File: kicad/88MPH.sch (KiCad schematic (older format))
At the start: 22 parts, among them CON1 AVR-ISP-6, IC1 ATMEGA328P-P, P1 CONN_01X04, Q1 Q_NPN_EBC, Q2 Q_NPN_EBC

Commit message: Full layout
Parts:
- BTN_1: renamed from BTN_A; footprint (none) -> Buttons_Switches_ThroughHole:SW_PUSH_6mm
- BTN_2: renamed from BTN_B; footprint (none) -> Buttons_Switches_ThroughHole:SW_PUSH_6mm
- C1: footprint (none) -> Capacitors_ThroughHole:C_Disc_D3_P2.5
- CON1: footprint AVR-ISP-6 -> misc:ICSP
- D1, D2: footprint MODULE -> misc:HDSP-816X
- IC1: footprint DIL28 -> misc:DIP28
- P1: footprint (none) -> misc:Strip_1x04
- PWR1: footprint (none) -> Buttons_Switches_ThroughHole:SW_Micro_SPST
- Q1, Q2: footprint (none) -> TO_SOT_Packages_THT:TO-92_Inline_Narrow_Oval
- R1, R10, R11, R2, R3, R4, R5, R6, R7, R8: footprint (none) -> misc:0.125_Resistor
- R9: value 150 -> 10K; footprint (none) -> misc:0.125_Resistor
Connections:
- net MISO: now also IC1.18 ((PCINT4/MISO)PB4), R5.2
- net MOSI: now also IC1.17 ((PCINT3/OC2A/MOSI)PB3), R4.2
- net SCK: now also IC1.19 ((PCINT5/SCK)PB5)
- net VCC: no longer C1.2, CON1.2, IC1.20 (AVCC), IC1.21 (AREF), IC1.7 (VCC), PWR1.2, R9.1
- new net 5V: C1.2, CON1.2, IC1.20 (AVCC), IC1.21 (AREF), IC1.7 (VCC), PWR1.2, R9.1
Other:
- moved on the sheet: R4, R5

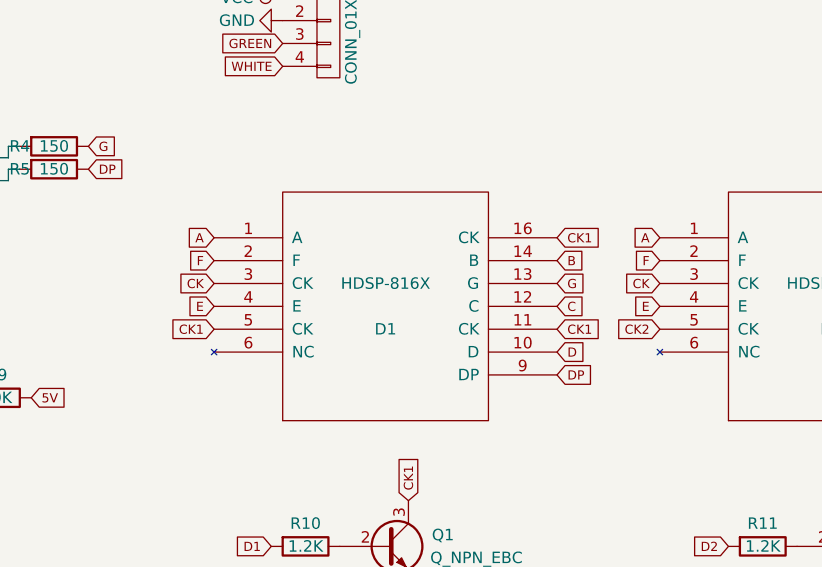
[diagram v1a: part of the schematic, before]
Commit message: Fixed cathode pin 3
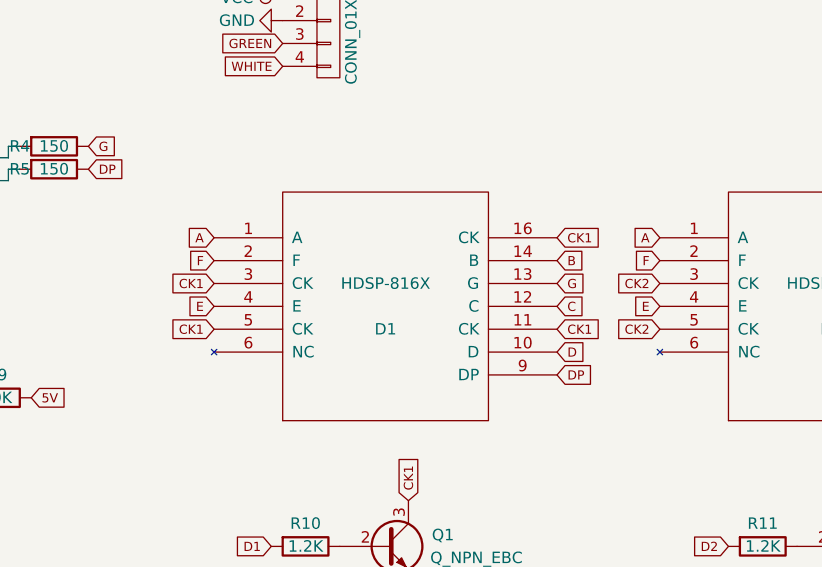
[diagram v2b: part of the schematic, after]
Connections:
- net CK1: now also D1.3 (CK)
- net CK2: now also D2.3 (CK)
- removed net CK: D1.3 (CK), D2.3 (CK)
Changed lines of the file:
@@
 F
 Text GLabel 5850 3050 0    40   Input ~ 0
-CK
+CK1
 Text GLabel 5850 3150 0    40   Input ~ 0
 E
@@
 F
 Text GLabel 7800 3050 0    40   Input ~ 0
-CK
+CK2
 Text GLabel 7800 3150 0    40   Input ~ 0
 E
